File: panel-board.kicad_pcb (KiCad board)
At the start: 4 copper layers, 281 x 195 mm, 322 parts, among them J1 Barrel_Jack_MountingPin, J2 RJ45, J3 Conn_02x05_Odd_Even, J4 Conn_02x04_Odd_Even, J5 Conn_01x04_Male, J6 Conn_01x04_Male, J7 Conn_01x04_Male, J8 Conn_01x04_Male, SW1 SW_Push, SW2 SW_Push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

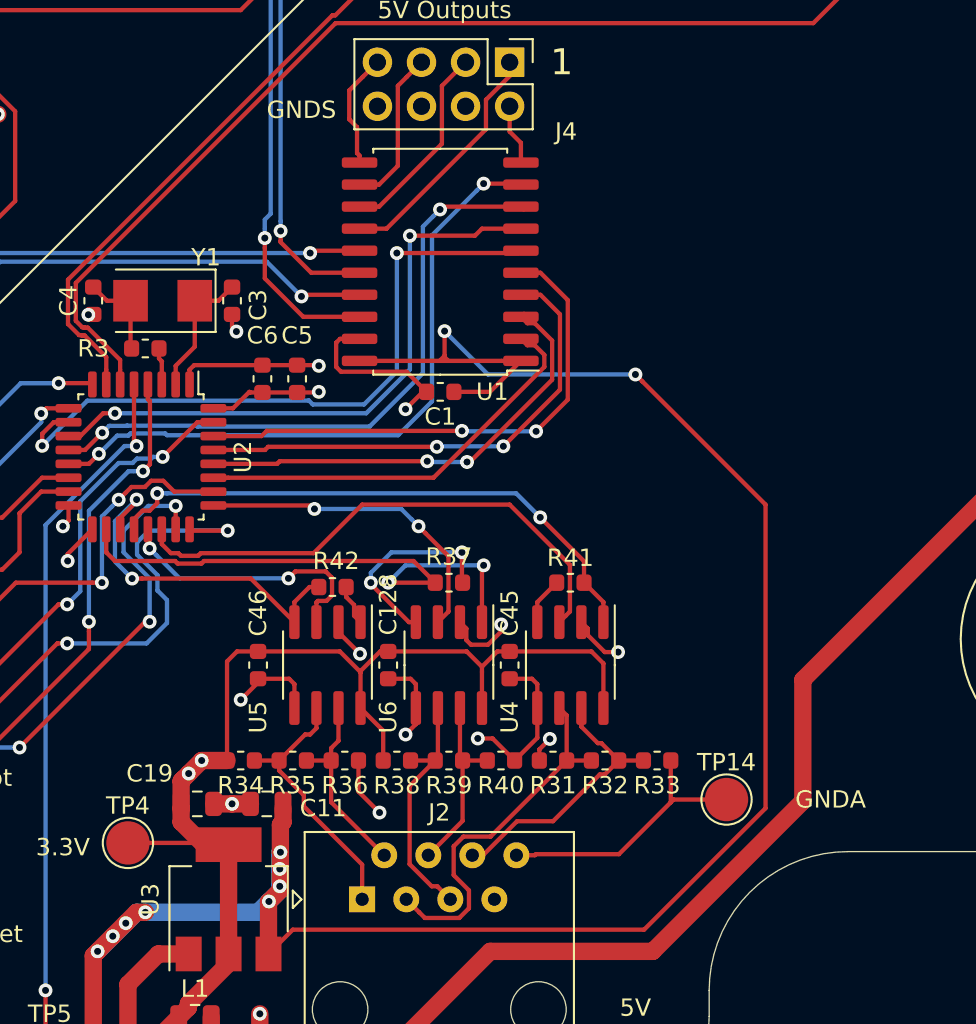
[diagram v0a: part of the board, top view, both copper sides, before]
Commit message: Finish PCB RS-485 fixes
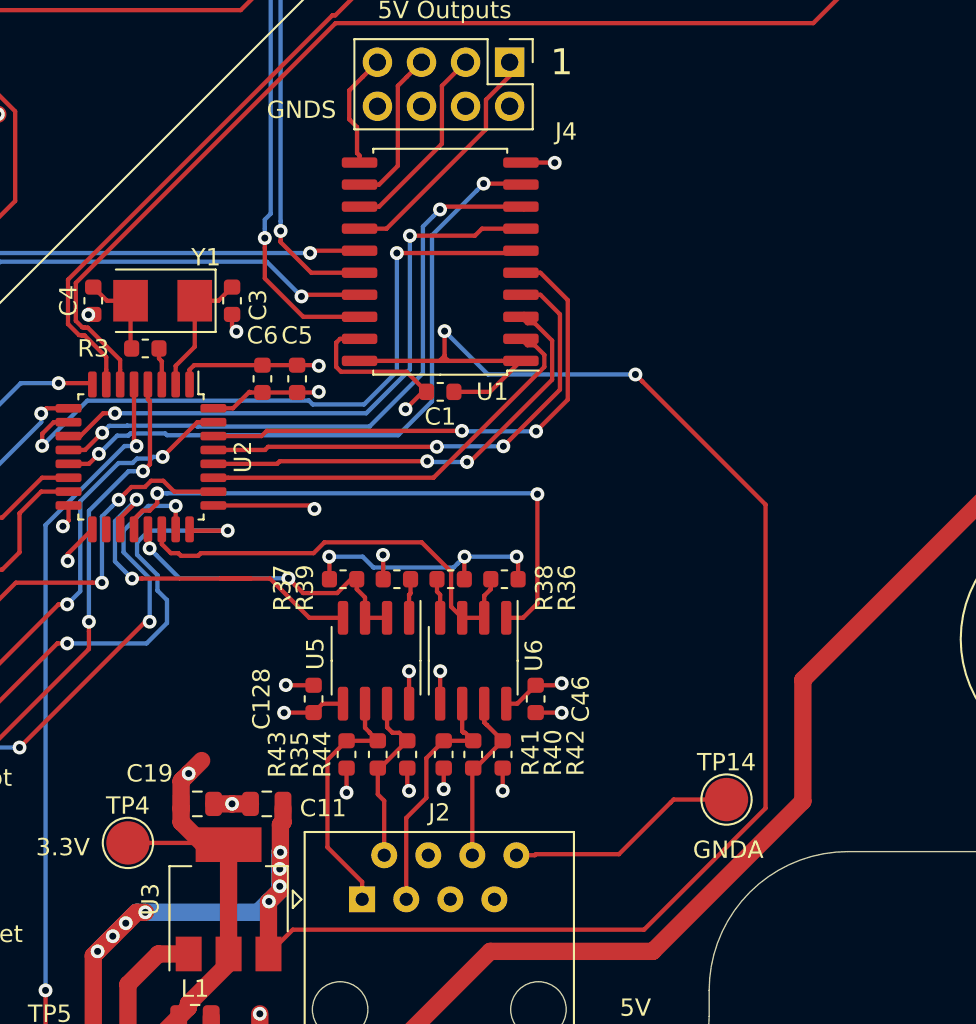
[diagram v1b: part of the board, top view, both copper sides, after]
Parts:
- removed C45: 0.1u, Capacitor_SMD:C_0603_1608Metric
- removed R31, R33, R34: 360R, Resistor_SMD:R_0603_1608Metric
- removed R32: 120R, Resistor_SMD:R_0603_1608Metric
- removed U4: SP3485EN, Package_SO:SOIC-8_3.9x4.9mm_P1.27mm
- added R43: 360R, Resistor_SMD:R_0603_1608Metric, F.Cu at (289.1, 219.4)
- added R44: 360R, Resistor_SMD:R_0603_1608Metric, F.Cu at (292.6, 219.4)
- R35: value 120R -> 100R
- R36, R38: value 360R -> 10k
- R37: value 0R -> 10k
- R39: value 120R -> 10k
- R40: value 360R -> 100R
- R41, R42: value 0R -> 360R
- moved C46 16.1 mm to (300.0, 216.2)
- moved R36 13.9 mm to (298.2, 209.3), turned to 0 degrees
- moved R42 13.8 mm to (298.1, 219.4), turned to 270 degrees
- moved R41 12.3 mm to (294.7, 219.4), turned to 270 degrees
- moved R38 10.9 mm to (295.1, 209.3), turned to 0 degrees
- moved R39 10.9 mm to (292.0, 209.3)
- moved R37 6.10 mm to (288.9, 209.3)
- moved R35 4.91 mm to (290.9, 219.4), turned to 90 degrees
- moved C128 4.72 mm to (287.2, 216.2)
- moved U5 2.81 mm to (290.8, 214.0)
- moved R40 1.64 mm to (296.4, 219.4), turned to 90 degrees
- moved U6 1.42 mm to (296.4, 214.0)
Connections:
- J2 pad 4: CK- -> Net-(J2-Pad4)
- J2 pad 5: CK+ -> Net-(J2-Pad5)
- R36 pad 1: GNDA -> RX_EN
- R36 pad 2: TX- -> GNDA
- R37 pad 1: Net-(R37-Pad1) -> TX_EN
- R37 pad 2: UART_CK -> GNDA
- R38 pad 1: CK+ -> Net-(R38-Pad1)
- R38 pad 2: +3V3 -> GNDA
- R39 pad 1: CK- -> Net-(R39-Pad1)
- R39 pad 2: CK+ -> +3V3
- R40 pad 1: GNDA -> RX-
- R40 pad 2: CK- -> RX+
- R41 pad 1: Net-(R41-Pad1) -> RX+
- R41 pad 2: UART_RX -> +3V3
- R42 pad 1: Net-(R42-Pad1) -> RX-
- R42 pad 2: UART_TX -> GNDA
- U2 pad 18: UART_CK -> Net-(U2-Pad18)
- U2 pad 25: CK_EN -> Net-(U2-Pad25)
- U5 pad 1: Net-(R42-Pad1) -> Net-(R39-Pad1)
- U5 pad 2: GNDA -> TX_EN
- U6 pad 1: UART_CK -> UART_RX
- U6 pad 2: GNDA -> RX_EN
- U6 pad 3: CK_EN -> RX_EN
- U6 pad 4: Net-(R37-Pad1) -> Net-(R38-Pad1)
- U6 pad 6: CK+ -> RX+
- U6 pad 7: CK- -> RX-
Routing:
- net UART_CK: track 33.1 -> 0.00 mm, vias 2 -> 0
- net +3V3: track 99.5 -> 67.5 mm, vias 5 -> 9
- net CK_EN: track 18.8 -> 0.00 mm, vias 2 -> 0
- net CK+: track 14.3 -> 0.00 mm
- net Net-(R37-Pad1): track 11.7 -> 0.00 mm, vias 2 -> 0
- net GNDA: track 270.1 -> 259.0 mm, vias 27 -> 29
- net CK-: track 10.8 -> 0.00 mm
- net RX+: track 21.4 -> 14.2 mm
- net Net-(U2-Pad25): track 0.00 -> 5.91 mm, vias 0 -> 1
- net RX-: track 16.2 -> 10.6 mm
- net RX_EN: track 30.9 -> 25.4 mm
- net Net-(R41-Pad1): track 2.74 -> 0.00 mm
- net Net-(R42-Pad1): track 2.37 -> 0.00 mm
- net Net-(R38-Pad1): track 0.00 -> 2.30 mm
- net TX_EN: track 15.9 -> 18.2 mm
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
